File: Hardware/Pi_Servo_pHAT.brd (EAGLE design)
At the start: 65 x 30 mm, 148 parts, among them J1 RASPBERRYPI-40-PIN-GPIO, J19 QWIIC, J20 USB C, J21 RVR, Q1 310mA/60V/1.6Ω, Q12 20V/4.2A/52mΩ/1.4W, Q2 20V/4.2A/52mΩ/1.4W, Q4 310mA/60V/1.6Ω, Q5 20V/4.2A/52mΩ/1.4W, Q7 20V/4.2A/52mΩ/1.4W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

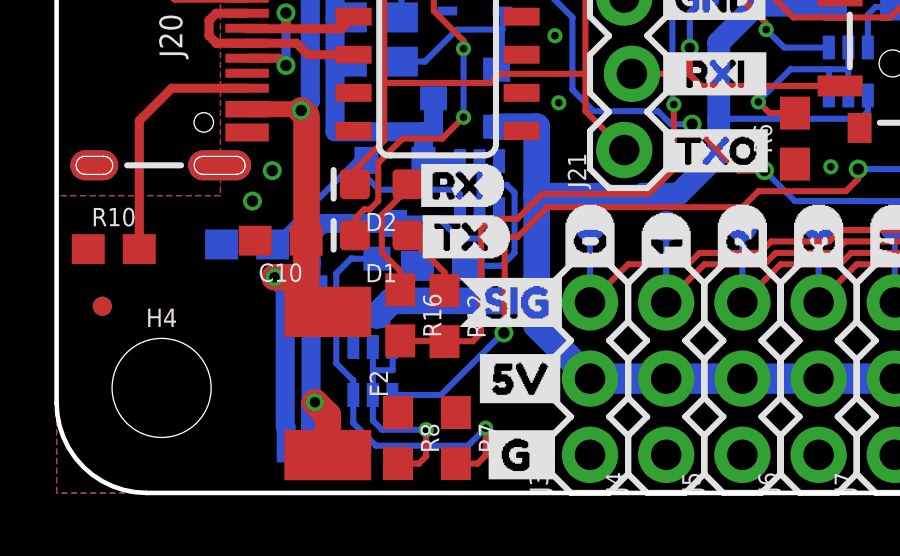
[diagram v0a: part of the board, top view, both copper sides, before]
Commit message: Updating resistor values for LEDs
330 for green and 1K for yellow.
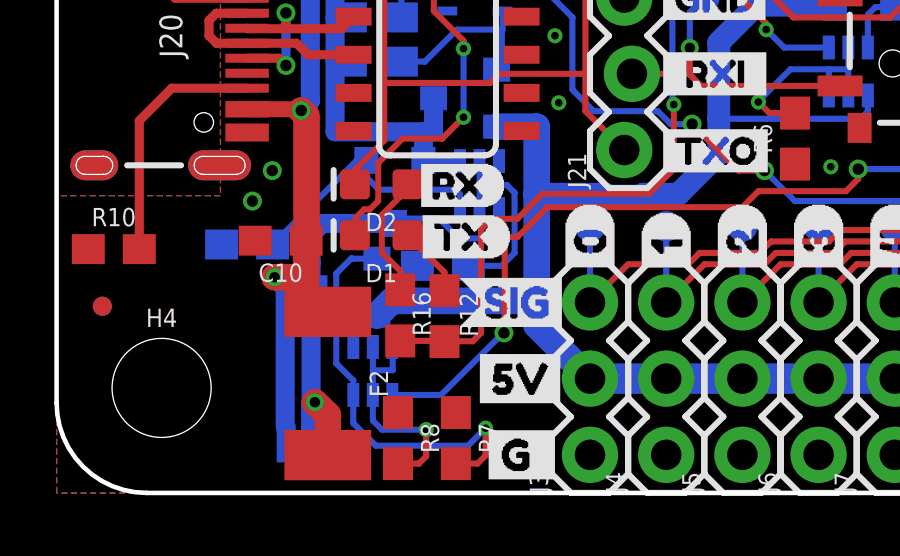
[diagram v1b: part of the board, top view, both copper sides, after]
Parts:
- R12: value 4.7k -> 330
- R16: value 4.7k -> 1k
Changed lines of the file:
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@@
 <?xml version="1.0" encoding="utf-8"?>
 <!DOCTYPE eagle SYSTEM "eagle.dtd">
-<eagle version="9.4.0">
+<eagle version="9.4.2">
 <drawing>
 <settings>
@@
 <layers>
 <layer number="1" name="Top" color="4" fill="1" visible="yes" active="yes"/>
-<layer number="16" name="Bottom" color="1" fill="1" visible="yes" active="yes"/>
+<layer number="16" name="Bottom" color="1" fill="1" visible="no" active="yes"/>
 <layer number="17" name="Pads" color="2" fill="1" visible="yes" active="yes"/>
 <layer number="18" name="Vias" color="2" fill="1" visible="yes" active="yes"/>
 <layer number="19" name="Unrouted" color="6" fill="1" visible="yes" active="yes"/>
 <layer number="20" name="Dimension" color="24" fill="1" visible="yes" active="yes"/>
-<layer number="21" name="tPlace" color="16" fill="1" visible="yes" active="yes"/>
+<layer number="21" name="tPlace" color="16" fill="1" visible="no" active="yes"/>
 <layer number="22" name="bPlace" color="14" fill="1" visible="no" active="yes"/>
-<layer number="23" name="tOrigins" color="15" fill="1" visible="yes" active="yes"/>
-<layer number="24" name="bOrigins" color="15" fill="1" visible="yes" active="yes"/>
-<layer number="25" name="tNames" color="7" fill="1" visible="no" active="yes"/>
+<layer number="23" name="tOrigins" color="15" fill="1" visible="no" active="yes"/>
+<layer number="24" name="bOrigins" color="15" fill="1" visible="no" active="yes"/>
+<layer number="25" name="tNames" color="7" fill="1" visible="yes" active="yes"/>
 <layer number="26" name="bNames" color="7" fill="1" visible="no" active="yes"/>
 <layer number="27" name="tValues" color="7" fill="1" visible="no" active="yes"/>
@@
 <layer number="49" name="Reference" color="13" fill="1" visible="no" active="yes"/>
 <layer number="50" name="dxf" color="7" fill="1" visible="no" active="yes"/>
-<layer number="51" name="tDocu" color="6" fill="1" visible="no" active="yes"/>
+<layer number="51" name="tDocu" color="6" fill="1" visible="yes" active="yes"/>
 <layer number="52" name="bDocu" color="7" fill="1" visible="no" active="yes"/>
 <layer number="91" name="Nets" color="2" fill="1" visible="no" active="no"/>
@@
 <attribute name="VALUE" x="9.2456" y="19.8628" size="0.6096" layer="27" font="vector" ratio="20" rot="R90" align="top-center"/>
 </element>
-<element name="R12" library="SparkFun-Resistors" package="0603" value="4.7k" x="12.9286" y="5.8928" smashed="yes" rot="R270">
-<attribute name="NAME" x="13.6906" y="5.8928" size="0.6096" layer="25" font="vector" ratio="20" rot="R270" align="bottom-center"/>
-<attribute name="PROD_ID" value="RES-07857" x="19.2786" y="9.7028" size="1.778" layer="27" font="vector" ratio="15" rot="R270" display="off"/>
-<attribute name="VALUE" x="12.1666" y="5.8928" size="0.6096" layer="27" font="vector" ratio="20" rot="R270" align="top-center"/>
-</element>
-<element name="R16" library="SparkFun-Resistors" package="0603" value="4.7k" x="11.4554" y="5.9182" smashed="yes" rot="R270">
-<attribute name="NAME" x="12.2174" y="5.9182" size="0.6096" layer="25" font="vector" ratio="20" rot="R270" align="bottom-center"/>
-<attribute name="PROD_ID" value="RES-07857" x="10.1854" y="13.5382" size="1.778" layer="27" font="vector" ratio="15" rot="R270" display="off"/>
-<attribute name="VALUE" x="10.6934" y="5.9182" size="0.6096" layer="27" font="vector" ratio="20" rot="R270" align="top-center"/>
+<element name="R12" library="SparkFun-Resistors" package="0603" value="330" x="12.9286" y="5.8928" smashed="yes" rot="R270">
+<attribute name="NAME" x="13.4366" y="5.9436" size="0.6096" layer="25" font="vector" ratio="20" rot="R270" align="bottom-center"/>
+<attribute name="PROD_ID" value="RES-00818" x="19.2786" y="9.7028" size="1.778" layer="27" font="vector" ratio="15" rot="R270" display="off"/>
+<attribute name="VALUE" value="330" x="12.1666" y="5.8928" size="0.6096" layer="27" font="vector" ratio="20" rot="R270" align="top-center"/>
+</element>
+<element name="R16" library="SparkFun-Resistors" package="0603" value="1k" x="11.4554" y="5.9182" smashed="yes" rot="R270">
+<attribute name="NAME" x="11.8618" y="5.969" size="0.6096" layer="25" font="vector" ratio="20" rot="R270" align="bottom-center"/>
+<attribute name="PROD_ID" value="RES-07856" x="10.1854" y="13.5382" size="1.778" layer="27" font="vector" ratio="15" rot="R270" display="off"/>
+<attribute name="VALUE" value="1k" x="10.6934" y="5.9182" size="0.6096" layer="27" font="vector" ratio="20" rot="R270" align="top-center"/>
 </element>
 <element name="J20" library="SparkFun-Connectors" package="USB-C-16P" value="USB C" x="6.35" y="15.24" smashed="yes" rot="R270">
